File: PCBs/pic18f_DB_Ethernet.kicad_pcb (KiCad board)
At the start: 2 copper layers, 100 x 62.3 mm, 33 parts, among them J1 OC1, J2 PicKIT 3, J3 IC1, J8 RJ45, SW1 SW_DPDT_x2, SW2 PWR_SW, U1 pic18f45k20

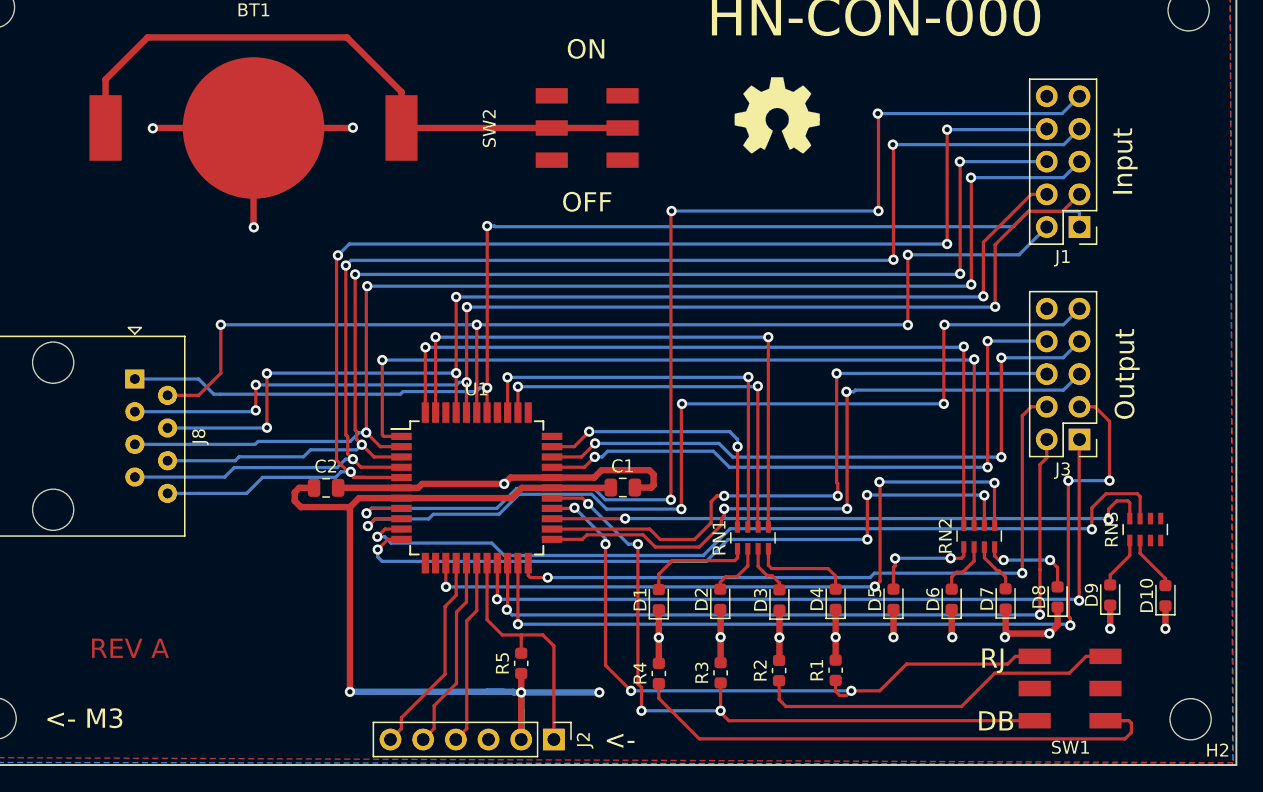
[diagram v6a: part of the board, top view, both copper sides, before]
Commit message: addressing hardware problems on PCB design. Pull downs missing and while a breakout works for prototyping code, it is time to commit the changes in FR4.
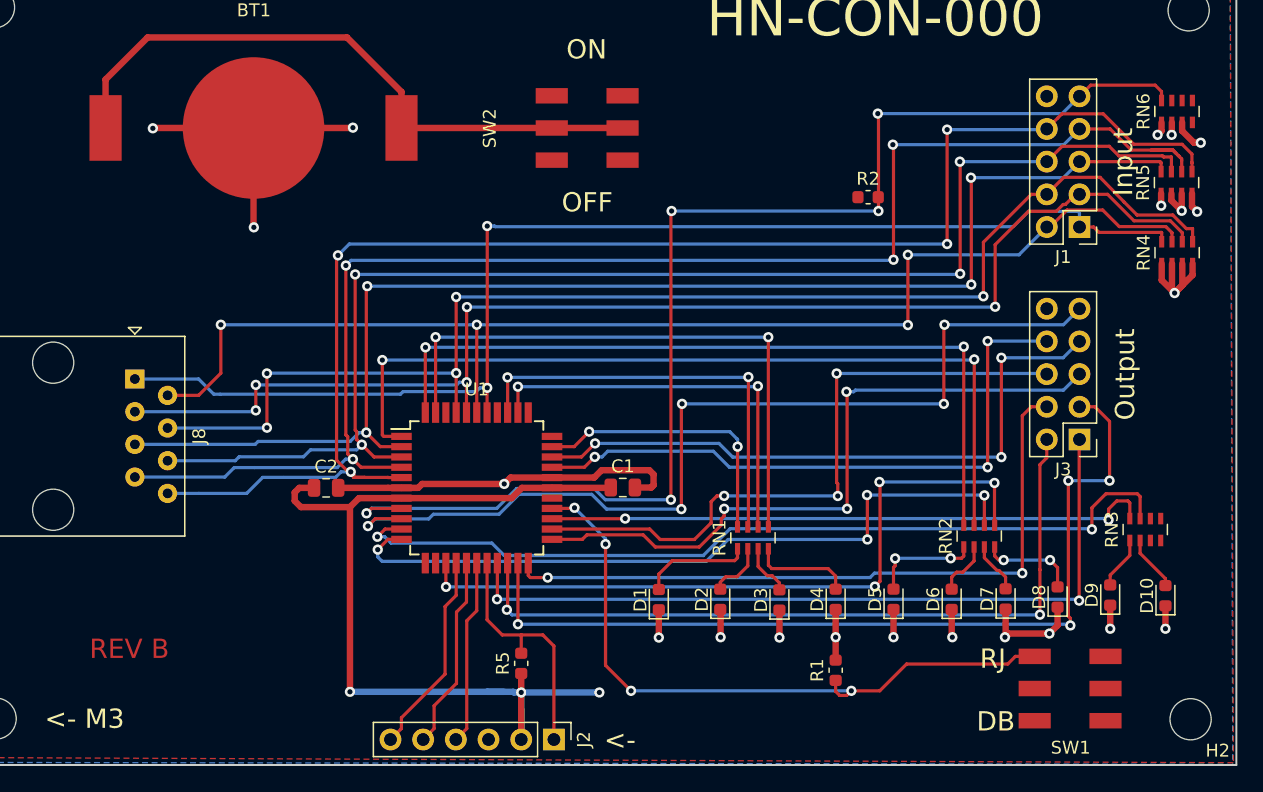
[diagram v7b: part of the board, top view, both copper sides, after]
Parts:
- removed R3, R4: R_US, Resistor_SMD:R_0603_1608Metric
- removed REF**: OSHW-Symbol_6.7x6mm_SilkScreen, Symbol:OSHW-Symbol_6.7x6mm_SilkScreen
- added RN4: 1.1K, Resistor_SMD:R_Array_Concave_4x0603, F.Cu at (195.4, 107.5)
- added RN5: 1.1K, Resistor_SMD:R_Array_Concave_4x0603, F.Cu at (195.4, 102.1)
- added RN6: 1.1K, Resistor_SMD:R_Array_Concave_4x0603, F.Cu at (195.4, 96.5)
- moved R2 37.4 mm to (171.4, 103.2), turned to 0 degrees
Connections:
- R2 pad 1: Net-(R2-Pad1) -> SW0
- SW1 pad 1: SW0 -> Net-(SW1-Pad1)
- SW1 pad 4: Net-(R4-Pad1) -> (no net)
- SW1 pad 5: 3v3 -> (no net)
- SW1 pad 6: Net-(R2-Pad1) -> (no net)
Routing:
- net SW0: track 54.3 -> 0.00 mm, vias 4 -> 0
- net Net-(R4-Pad1): track 42.2 -> 0.00 mm
- net Net-(R2-Pad1): track 28.7 -> 0.00 mm
- net GND: track 83.1 -> 97.9 mm, vias 14 -> 21
- net In4: track 87.3 -> 101.9 mm
- net In8: track 102.0 -> 116.5 mm
- net In7: track 103.5 -> 115.7 mm
- net In2: track 86.0 -> 97.7 mm
- net In6: track 95.1 -> 106.7 mm
- net In3: track 90.2 -> 100.1 mm
- net In9: track 90.1 -> 97.7 mm
- net In1: track 90.3 -> 97.5 mm
- net In5: track 97.2 -> 104.3 mm
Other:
- board text added: "REV B"
- board text removed: "REV A"

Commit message: Finished REV B design.
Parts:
- removed R1, R2: R_US, Resistor_SMD:R_0603_1608Metric
- added SW3: SW_Push, SPST_Button_FSM2JRT:SPST_Button_FSM2JRT, F.Cu at (161.7, 96.7)
- moved RN4 76.4 mm to (125.7, 138.8)
- moved RN5 75.8 mm to (125.7, 132.0)
- moved RN6 27.1 mm to (168.6, 101.2), turned to 0 degrees
- moved J3 1.46 mm to (187.8, 123.5)
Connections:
- RN3 pad 3: Net-(RN3-Pad3) -> GND
- RN3 pad 6: Net-(RN3-Pad6) -> SW1
- RN4 pad 5: In4 -> In1
- RN4 pad 6: In3 -> In2
- RN4 pad 7: In2 -> In3
- RN4 pad 8: In1 -> In4
- RN5 pad 5: In8 -> In5
- RN5 pad 6: In7 -> In6
- RN5 pad 7: In6 -> In7
- RN5 pad 8: In5 -> In8
- RN6 pad 4: Net-(RN6-Pad4) -> GND
- RN6 pad 5: Net-(RN6-Pad5) -> In9
- RN6 pad 6: Net-(RN6-Pad6) -> SW0
- RN6 pad 8: In9 -> Net-(RN6-Pad8)
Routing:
- net SW0: track 0.00 -> 57.7 mm, vias 0 -> 2
- net SW1: track 52.6 -> 73.2 mm, vias 4 -> 6
- net In1: track 97.5 -> 112.7 mm, vias 2 -> 3
- net 3v3: track 73.9 -> 87.5 mm
- net In2: track 97.7 -> 110.9 mm, vias 4 -> 5
- net In3: track 100.1 -> 111.0 mm, vias 5 -> 6
- net In8: track 116.5 -> 107.6 mm, vias 4 -> 5
- net GND: track 97.9 -> 106.4 mm, vias 21 -> 20
- net In4: track 101.9 -> 109.6 mm
- net In9: track 97.7 -> 92.7 mm
- net In7: track 115.7 -> 111.4 mm, vias 4 -> 5
- net In6: track 106.7 -> 103.6 mm, vias 4 -> 5
- net Out3: track 69.6 -> 67.0 mm
- net Out6: track 50.8 -> 48.3 mm
- net In5: track 104.3 -> 106.5 mm, vias 4 -> 5
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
